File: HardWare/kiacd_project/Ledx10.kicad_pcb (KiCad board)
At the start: 2 copper layers, 90 x 100.5 mm, 49 parts, among them J1 POWER_IN, U1 TPS923651

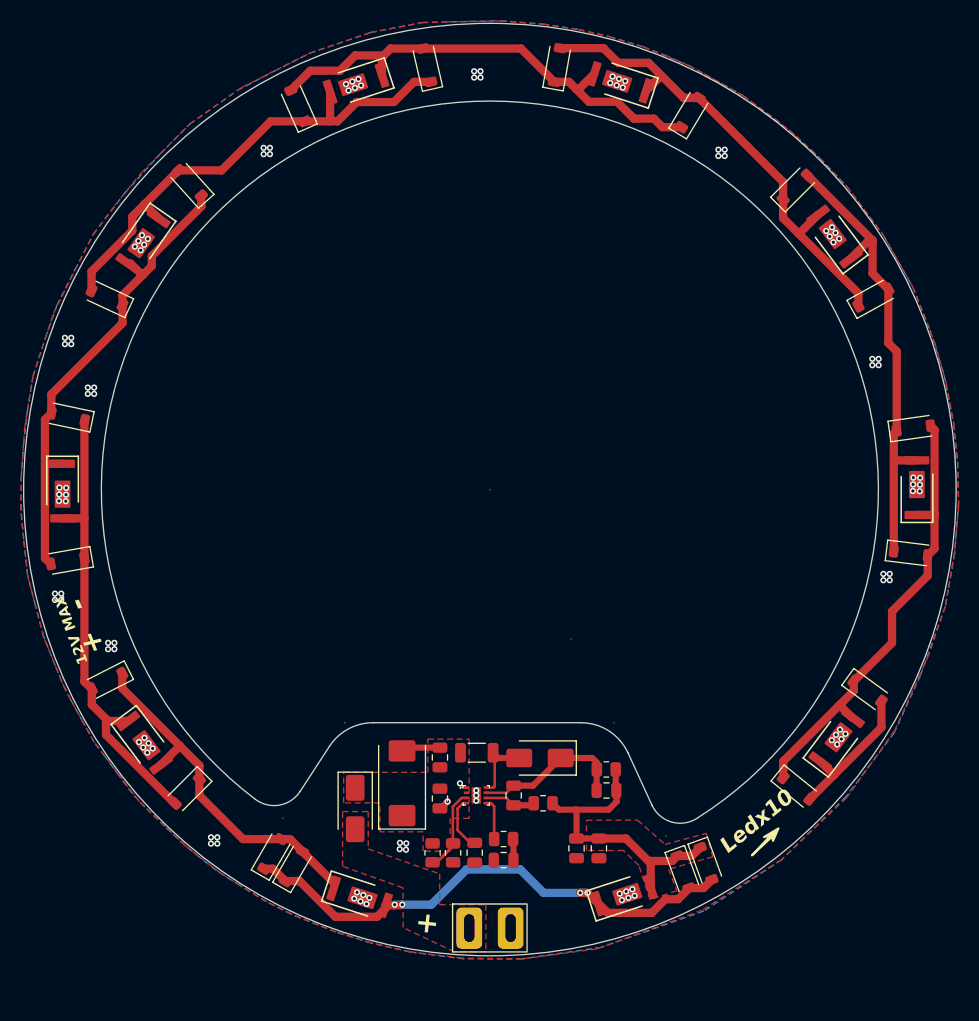
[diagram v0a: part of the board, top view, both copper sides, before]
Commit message: 更新 PCB 铺铜，和泪滴
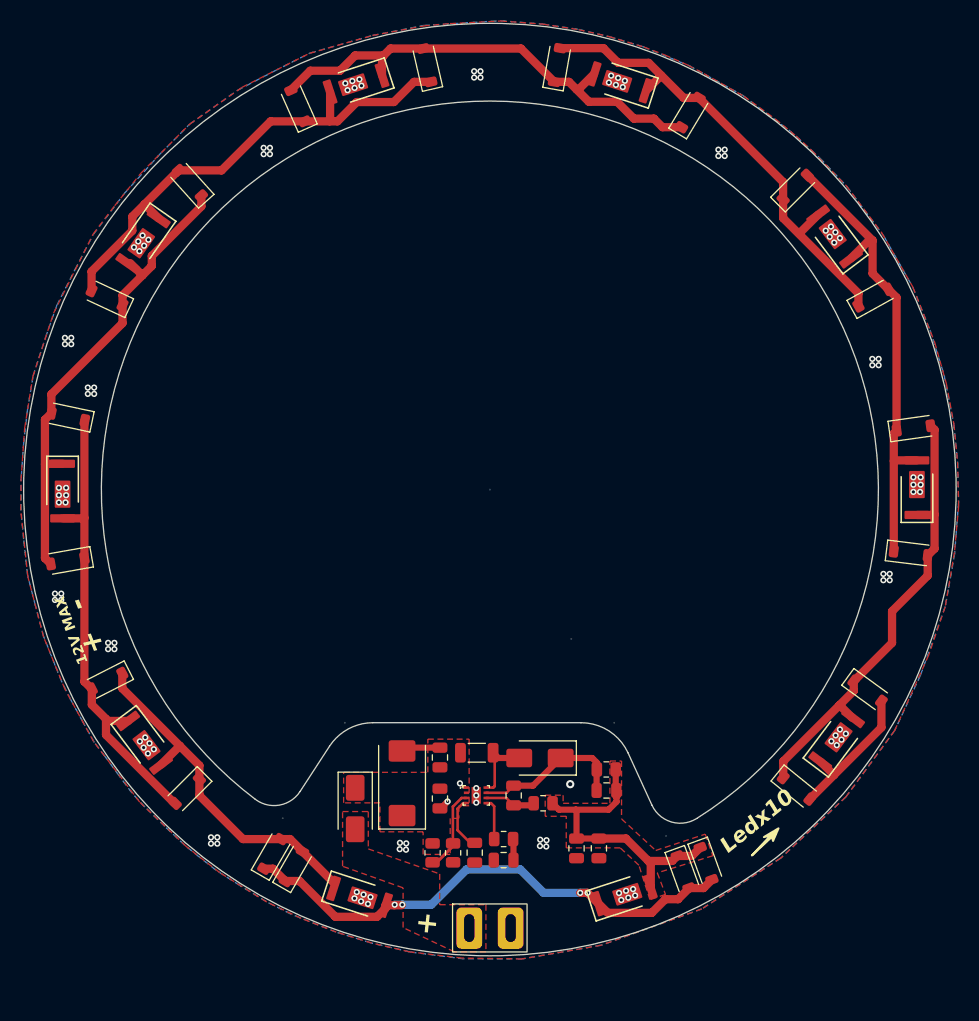
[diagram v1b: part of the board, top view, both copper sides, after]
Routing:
- net GND: vias 109 -> 114

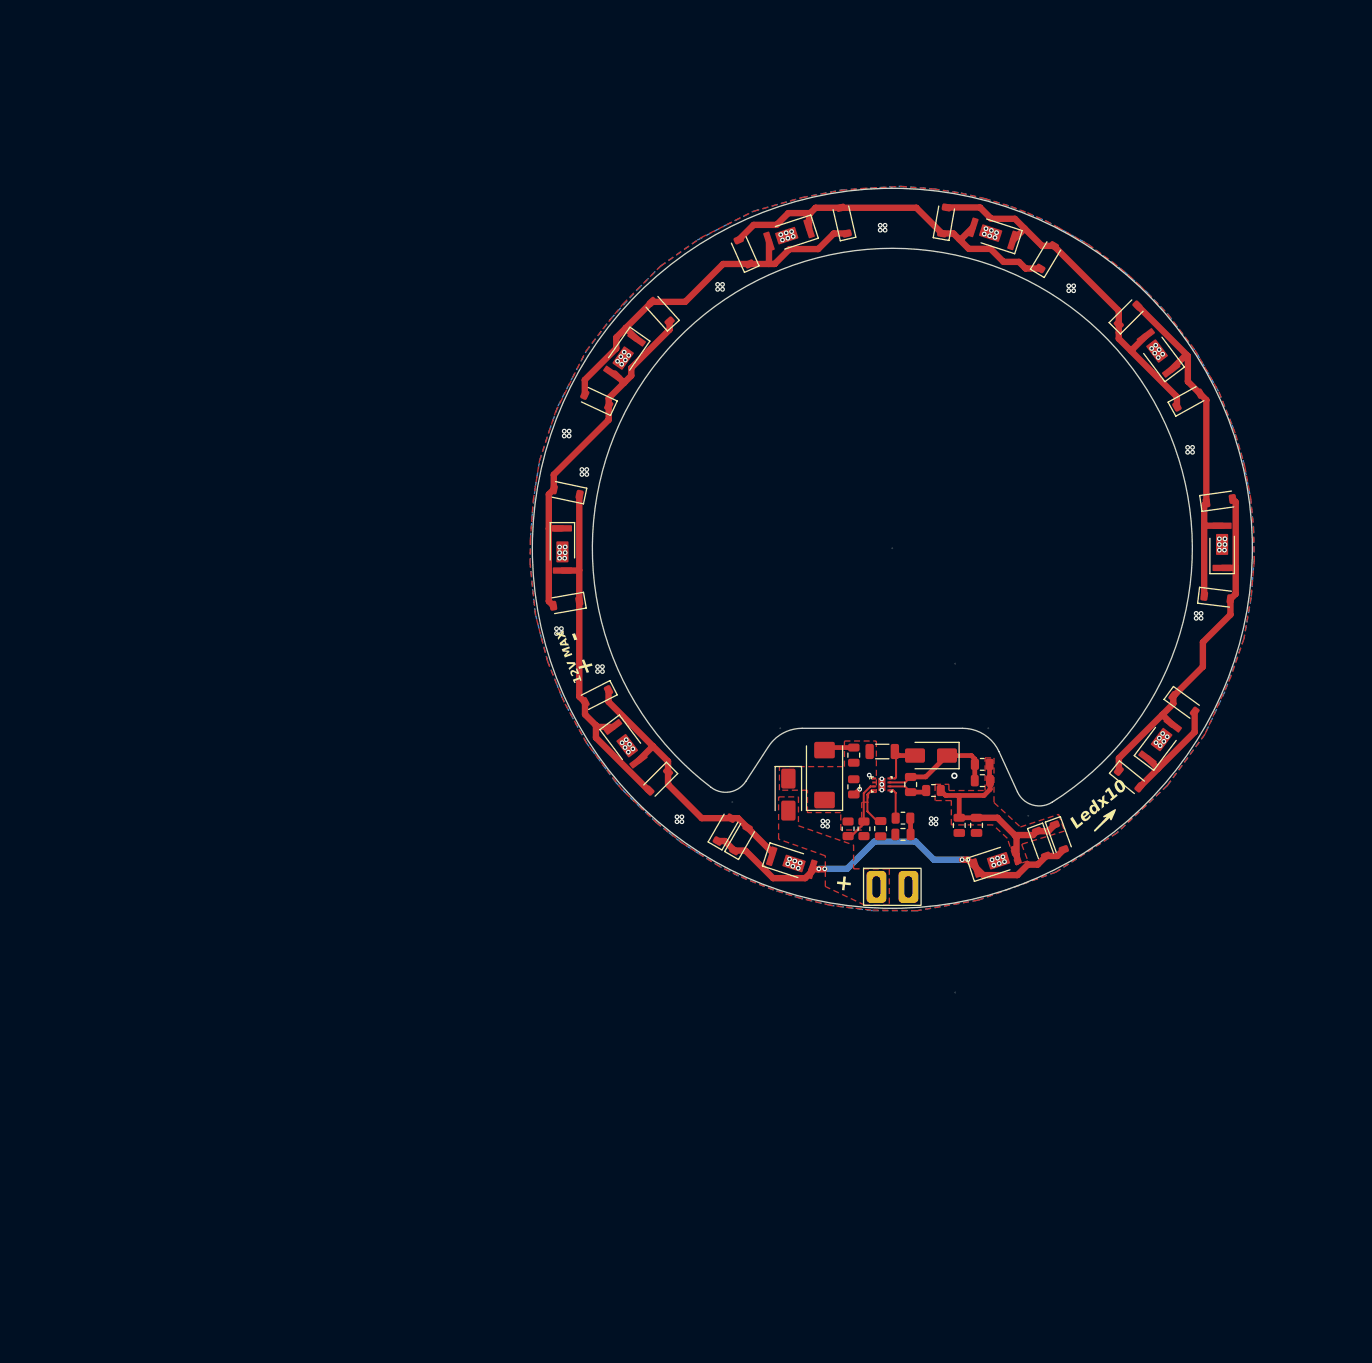
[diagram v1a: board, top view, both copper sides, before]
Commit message: 更新电路设计LED增加到20pix
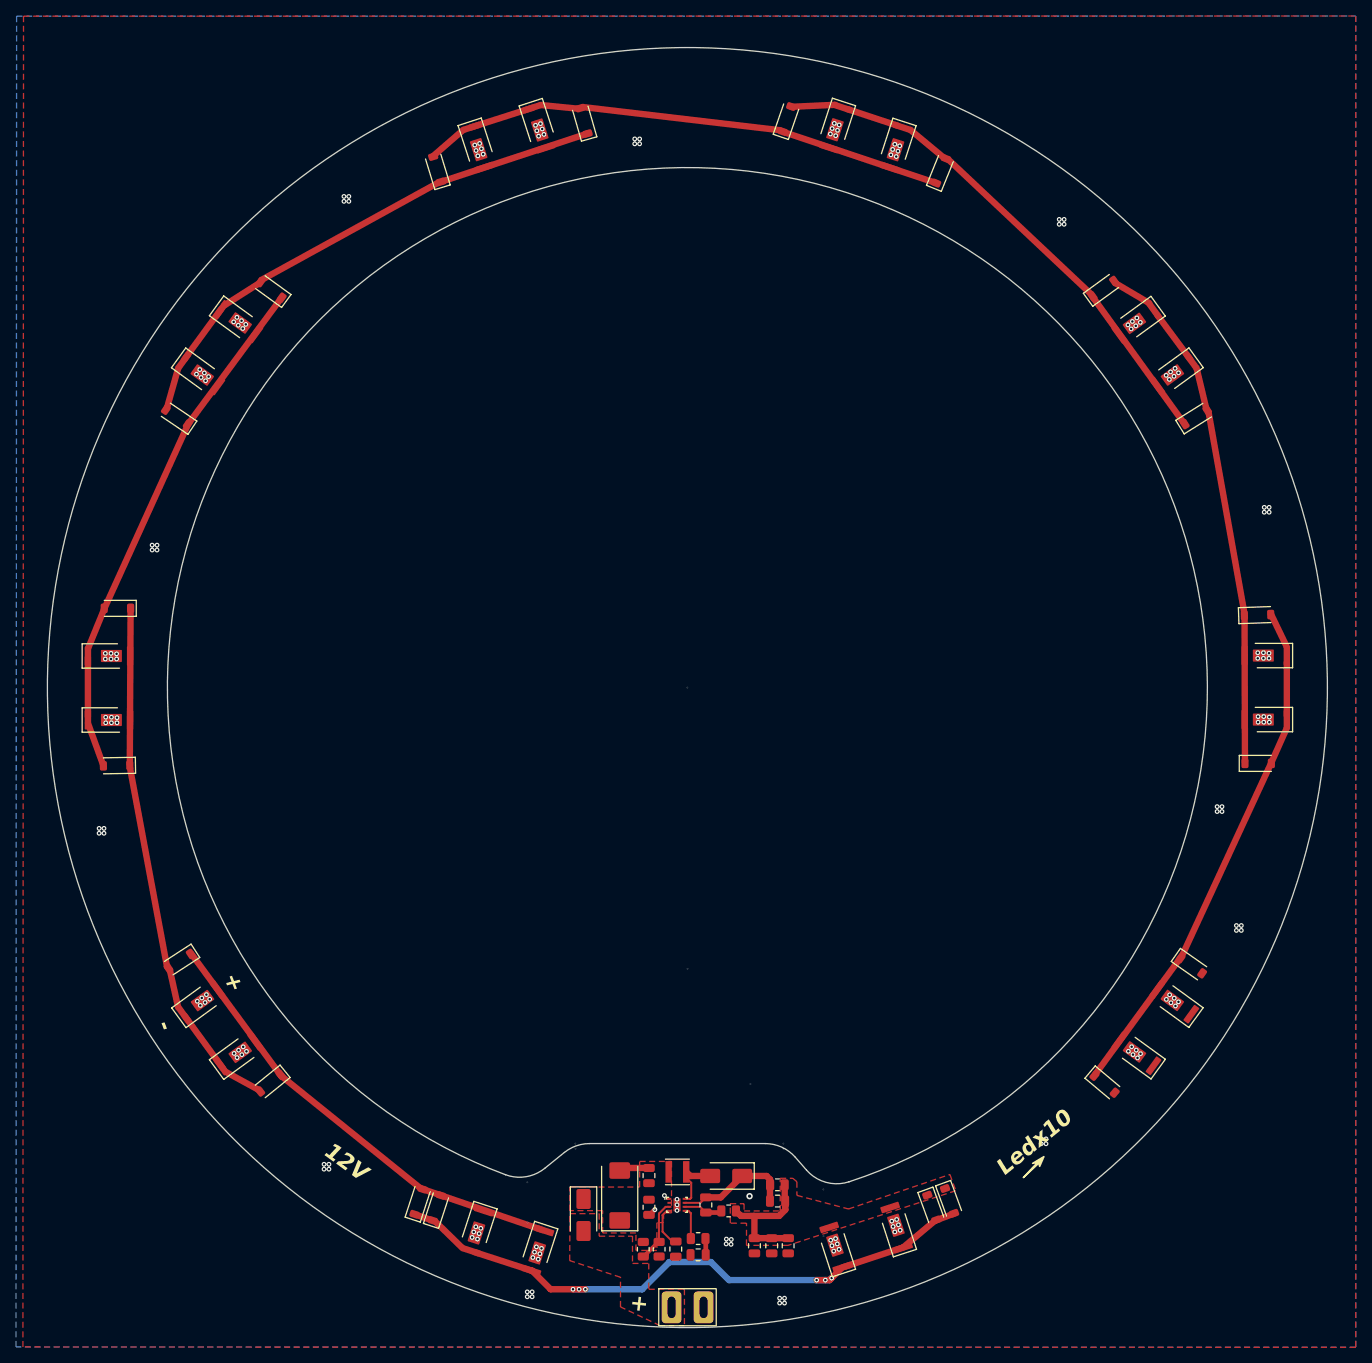
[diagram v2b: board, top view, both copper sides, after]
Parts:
- added C10: 10uF,100V, Capacitor_SMD:C_0805_2012Metric, F.Cu at (110.4, 167.2)
- added D33: 5730D34W, 3rd_LED_SMD:LED5730_2012Metric, F.Cu at (158.4, 136.5)
- added D34: 5730D34W, 3rd_LED_SMD:LED5730_2012Metric, F.Cu at (169.8, 93.4)
- added D35: 5730D34W, 3rd_LED_SMD:LED5730_2012Metric, F.Cu at (153.7, 51.9)
- added D36: 5730D34W, 3rd_LED_SMD:LED5730_2012Metric, F.Cu at (116.3, 27.7)
- added D37: 5730D34W, 3rd_LED_SMD:LED5730_2012Metric, F.Cu at (71.7, 30.1)
- added D38: 5730D34W, 3rd_LED_SMD:LED5730_2012Metric, F.Cu at (37.2, 58.3)
- added D39: 5730D34W, 3rd_LED_SMD:LED5730_2012Metric, F.Cu at (25.8, 101.4)
- added D40: 5730D34W, 3rd_LED_SMD:LED5730_2012Metric, F.Cu at (41.9, 143.0)
- added D41: 5730D34W, 3rd_LED_SMD:LED5730_2012Metric, F.Cu at (79.0, 168.1)
- added D42: 5730D34W, 3rd_LED_SMD:LED5730_2012Metric, F.Cu at (123.9, 164.6)
- L1: footprint Inductor_SMD:L_1206_3216Metric -> Inductor_SMD:L_Taiyo-Yuden_MD-3030
- moved D7 61.9 mm to (37.2, 136.5), turned to 36 degrees
- moved D9 61.8 mm to (34.3, 131.6), turned to -147 degrees
- moved D8 61.5 mm to (45.7, 146.8), turned to -141 degrees
- moved D4 60.9 mm to (71.5, 165.6), turned to -108 degrees
- moved D5 60.2 mm to (64.2, 161.6), turned to 72 degrees
- moved D6 59.8 mm to (66.5, 162.4), turned to 72 degrees
- moved D12 59.8 mm to (26.5, 107.1), turned to -179 degrees
- moved D19 58.5 mm to (102.7, 158.4)
- moved R1 58.5 mm to (92.3, 167.6)
- moved R2 58.5 mm to (94.3, 167.6)
- moved R4 58.5 mm to (103.0, 162.8)
- moved C1 58.5 mm to (93.0, 158.4)
- moved C2 58.5 mm to (89.4, 160.9)
- moved C3 58.5 mm to (93.0, 162.3)
- moved C4 58.5 mm to (96.4, 167.6)
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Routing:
- net Net-(D13-K): track 47.7 -> 0.00 mm
- net Net-(D16-K): track 46.8 -> 0.00 mm
- net Net-(D20-K): track 46.5 -> 0.00 mm
- net Net-(D10-K): track 45.7 -> 0.00 mm
- net Net-(D23-K): track 45.0 -> 0.00 mm
- net Net-(D10-A): track 44.8 -> 0.00 mm
- net Net-(D26-K): track 43.9 -> 0.00 mm
- net Net-(D4-K): track 33.8 -> 0.00 mm
- net GND: track 19.8 -> 5.59 mm, vias 114 -> 178
- net /LED+: track 28.7 -> 16.9 mm
- net Net-(D1-K): track 51.8 -> 46.3 mm, vias 4 -> 6
- net Net-(D19-A): track 6.91 -> 7.58 mm
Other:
- board size 90 x 100.5 mm -> 160 x 160 mm
- board text added: "12V"
- board text removed: "12V MAX"

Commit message: 更新PCB设计，增加LED并联，增强光照强度
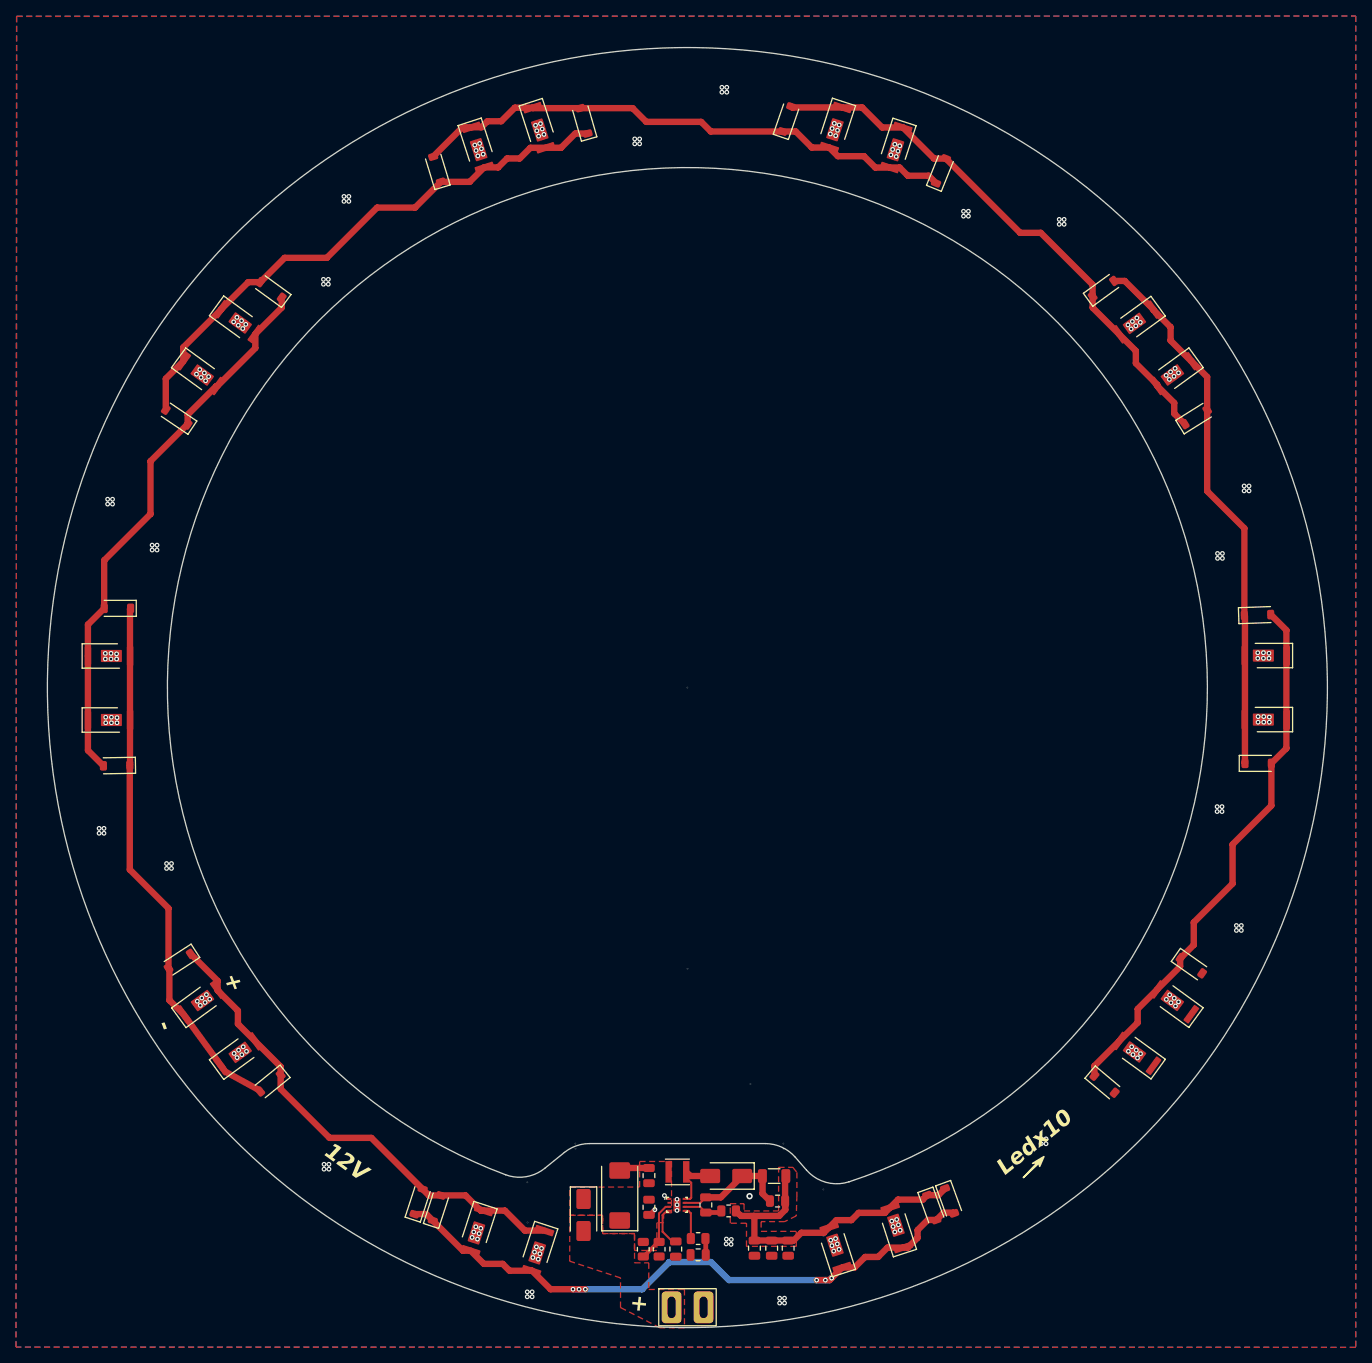
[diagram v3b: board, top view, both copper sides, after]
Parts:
- R5: value 1000mR -> 500mR; footprint Resistor_SMD:R_0805_2012Metric -> Resistor_SMD:R_1206_3216Metric
- moved R5 1.17 mm to (108.7, 158.4)
- moved C10 0.30 mm to (110.4, 167.5)
- moved C8 0.30 mm to (106.2, 167.5)
- moved C9 0.30 mm to (108.4, 167.5)
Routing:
- net Net-(D13-K): track 0.00 -> 70.3 mm
- net Net-(D10-K): track 0.00 -> 69.5 mm
- net Net-(D16-K): track 0.00 -> 69.3 mm
- net Net-(D20-K): track 0.00 -> 69.1 mm
- net Net-(D26-K): track 0.00 -> 68.4 mm
- net Net-(D23-K): track 0.00 -> 68.0 mm
- net Net-(D4-K): track 0.00 -> 61.9 mm
- net Net-(D10-A): track 0.00 -> 53.6 mm
- net Net-(D1-K): track 46.3 -> 81.3 mm
- net /LED+: track 16.9 -> 40.6 mm
- net GND: vias 178 -> 202
